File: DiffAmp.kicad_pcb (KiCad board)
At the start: 2 copper layers, 111 parts, among them J1 USB_OTG, J2 Screw_Terminal_1x03, J3 Conn_01x02, J4 Conn_01x02, J5 Conn_01x02, U1 SF_IHXXXXS, U2 TPS7A49, U3 TPS7A30, U4 OPA189, U5 AD8421, U6 OPA189, U7 OPA189

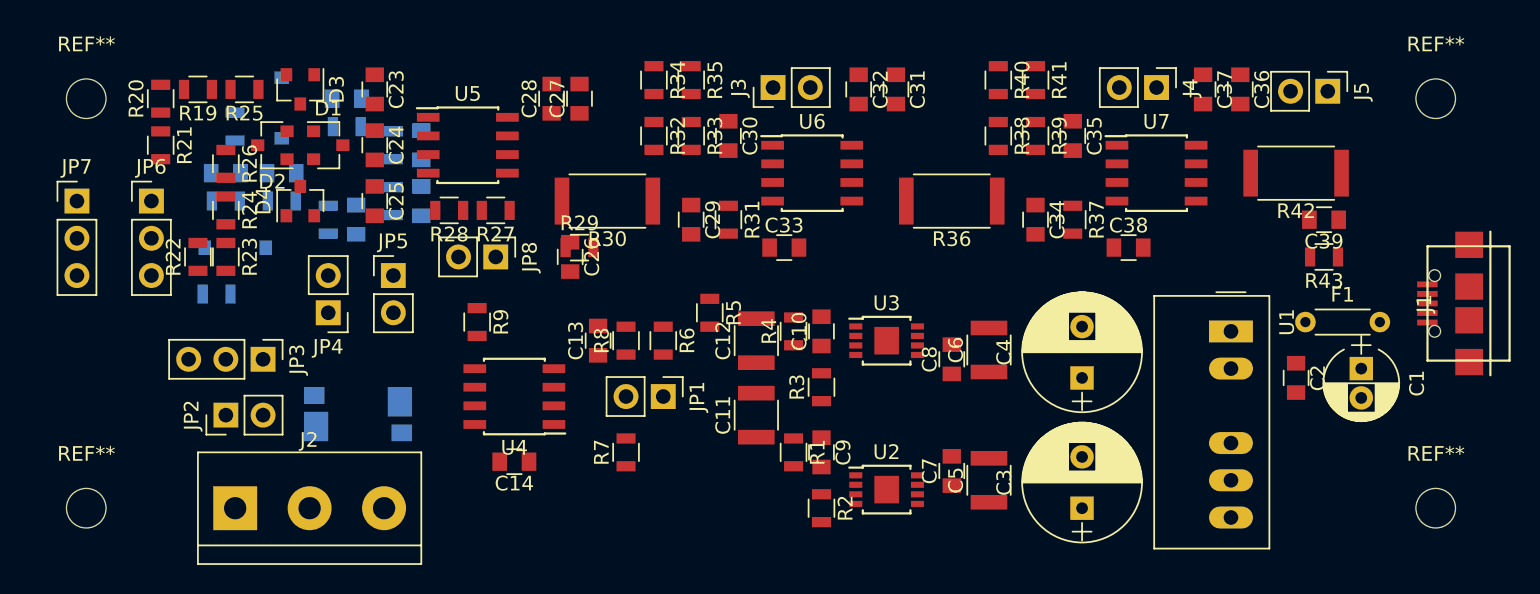
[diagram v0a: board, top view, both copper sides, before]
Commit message: Corrected Board Outline
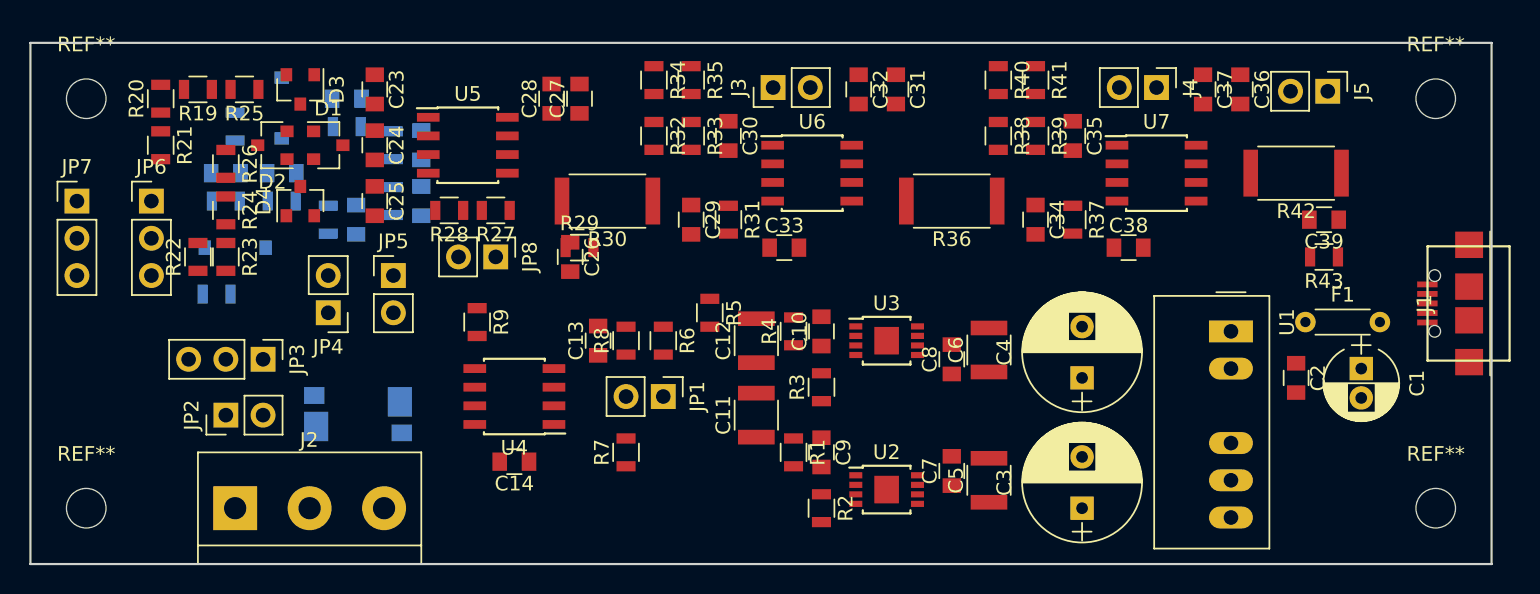
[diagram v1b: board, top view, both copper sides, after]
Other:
- board outline added: 99.7 x 35.6 mm
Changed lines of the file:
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@@
     (pad 1 np_thru_hole circle (at 0 0) (size 2.7 2.7) (drill 2.7) (layers *.Cu *.Mask))
   )
-  (gr_line (start 71.755 59.69) (end 171.45 59.69) (angle 90) (layer Eco2.User) (width 0.2))
-  (gr_line (start 71.755 95.25) (end 71.755 59.69) (angle 90) (layer Eco2.User) (width 0.2))
-  (gr_line (start 171.45 95.25) (end 71.755 95.25) (angle 90) (layer Eco2.User) (width 0.2))
-  (gr_line (start 171.45 95.25) (end 171.45 59.69) (angle 90) (layer Eco2.User) (width 0.2))
+  (gr_line (start 71.755 59.69) (end 71.755 95.25) (angle 90) (layer Edge.Cuts) (width 0.15))
+  (gr_line (start 171.45 59.69) (end 71.755 59.69) (angle 90) (layer Edge.Cuts) (width 0.15))
+  (gr_line (start 171.45 95.25) (end 171.45 59.69) (angle 90) (layer Edge.Cuts) (width 0.15))
+  (gr_line (start 71.755 95.25) (end 171.45 95.25) (angle 90) (layer Edge.Cuts) (width 0.15))
 )

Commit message: Begin Layouting
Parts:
- R10: moved to F.Cu
- moved C26 13.1 mm to (103.5, 62.2), turned to 0 degrees
- moved R10 3.17 mm to (97.8, 86.4)
- moved J3 2.67 mm to (125.1, 62.7), turned to 270 degrees
- moved JP8 2.54 mm to (101.0, 74.3), turned to 90 degrees
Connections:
- J5 pad 2: (no net) -> GNDA
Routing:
- net GNDA: track 0.00 -> 226.5 mm
- net Net-(C11-Pad2): track 0.00 -> 104.0 mm
- net VDDA: track 0.00 -> 62.7 mm
- net VSSA: track 0.00 -> 60.8 mm
- net Net-(C1-Pad2): track 0.00 -> 34.8 mm
- net Net-(JP5-Pad2): track 0.00 -> 31.7 mm, vias 0 -> 1
- net Net-(C4-Pad2): track 0.00 -> 31.6 mm
- net Net-(C3-Pad1): track 0.00 -> 26.7 mm
- net Net-(C20-Pad1): track 0.00 -> 22.2 mm
- net Net-(C35-Pad1): track 0.00 -> 21.6 mm
- net Net-(C30-Pad1): track 0.00 -> 21.4 mm
- net Net-(C24-Pad2): track 0.00 -> 20.1 mm
- net Net-(C1-Pad1): track 0.00 -> 18.6 mm
- net Net-(C23-Pad2): track 0.00 -> 18.3 mm
- net Net-(JP3-Pad2): track 0.00 -> 17.9 mm
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- added copper zone on F.Cu, net Net-(C11-Pad2)

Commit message: Layout Completed
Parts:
- added ?: , DiffAmp:VIA-0.6mm, F.Cu at (119.8, 68.8)
- added ?: , DiffAmp:VIA-0.6mm, F.Cu at (76.8, 74.9)
- added ?: , DiffAmp:VIA-0.6mm, F.Cu at (162.6, 64.8)
- added ?: , DiffAmp:VIA-0.6mm, F.Cu at (162.6, 68.6)
- added ?: , DiffAmp:VIA-0.6mm, F.Cu at (166.4, 68.6)
- added ?: , DiffAmp:VIA-0.6mm, F.Cu at (170.2, 68.6)
- added ?: , DiffAmp:VIA-0.6mm, F.Cu at (170.2, 64.8)
- added ?: , DiffAmp:VIA-0.6mm, F.Cu at (145.4, 61.0)
- added ?: , DiffAmp:VIA-0.6mm, F.Cu at (134.0, 61.0)
- added ?: , DiffAmp:VIA-0.6mm, F.Cu at (126.4, 61.0)
- added ?: , DiffAmp:VIA-0.6mm, F.Cu at (122.6, 61.0)
- added ?: , DiffAmp:VIA-0.6mm, F.Cu at (103.5, 61.0)
- added ?: , DiffAmp:VIA-0.6mm, F.Cu at (79.4, 78.1)
- added ?: , DiffAmp:VIA-0.6mm, F.Cu at (107.3, 61.0)
- added ?: , DiffAmp:VIA-0.6mm, F.Cu at (111.1, 61.0)
- added ?: , DiffAmp:VIA-0.6mm, F.Cu at (97.8, 61.6)
- added ?: , DiffAmp:VIA-0.6mm, F.Cu at (88.3, 61.0)
- added ?: , DiffAmp:VIA-0.6mm, F.Cu at (84.5, 61.0)
- added ?: , DiffAmp:VIA-0.6mm, F.Cu at (80.6, 61.0)
- added ?: , DiffAmp:VIA-0.6mm, F.Cu at (76.8, 61.0)
- added ?: , DiffAmp:VIA-0.6mm, F.Cu at (73.0, 61.0)
- added ?: , DiffAmp:VIA-0.6mm, F.Cu at (150.4, 61.9)
- added ?: , DiffAmp:VIA-0.6mm, F.Cu at (151.8, 61.0)
- added ?: , DiffAmp:VIA-0.6mm, F.Cu at (76.8, 78.1)
- added ?: , DiffAmp:VIA-0.6mm, F.Cu at (158.8, 61.0)
- added ?: , DiffAmp:VIA-0.6mm, F.Cu at (162.6, 61.0)
- added ?: , DiffAmp:VIA-0.6mm, F.Cu at (166.4, 61.0)
- added ?: , DiffAmp:VIA-0.6mm, F.Cu at (118.7, 85.1)
- added ?: , DiffAmp:VIA-0.6mm, F.Cu at (118.7, 82.5)
- added ?: , DiffAmp:VIA-0.6mm, F.Cu at (123.8, 82.5)
- added ?: , DiffAmp:VIA-0.6mm, F.Cu at (134.6, 83.8)
- added ?: , DiffAmp:VIA-0.6mm, F.Cu at (127.6, 82.5)
- added ?: , DiffAmp:VIA-0.6mm, F.Cu at (131.4, 82.5)
- added ?: , DiffAmp:VIA-0.6mm, F.Cu at (137.2, 83.8)
- added ?: , DiffAmp:VIA-0.6mm, F.Cu at (78.1, 74.9)
- added ?: , DiffAmp:VIA-0.6mm, F.Cu at (139.7, 83.8)
- added ?: , DiffAmp:VIA-0.6mm, F.Cu at (139.7, 81.3)
- added ?: , DiffAmp:VIA-0.6mm, F.Cu at (145.4, 81.3)
- added ? (x2): , DiffAmp:VIA-0.6mm, F.Cu at (142.9, 86.4)
- added ?: , DiffAmp:VIA-0.6mm, F.Cu at (139.1, 86.4)
- added ?: , DiffAmp:VIA-0.6mm, F.Cu at (135.3, 86.4)
- added ?: , DiffAmp:VIA-0.6mm, F.Cu at (131.4, 86.4)
- added ?: , DiffAmp:VIA-0.6mm, F.Cu at (120.0, 90.2)
- added ?: , DiffAmp:VIA-0.6mm, F.Cu at (123.8, 90.2)
- added ?: , DiffAmp:VIA-0.6mm, F.Cu at (78.7, 82.5)
- added ?: , DiffAmp:VIA-0.6mm, F.Cu at (123.8, 94.0)
- added ?: , DiffAmp:VIA-0.6mm, F.Cu at (127.6, 94.0)
- added ?: , DiffAmp:VIA-0.6mm, F.Cu at (131.4, 94.0)
- added ?: , DiffAmp:VIA-0.6mm, F.Cu at (135.3, 94.0)
- added ?: , DiffAmp:VIA-0.6mm, F.Cu at (139.1, 94.0)
- added ?: , DiffAmp:VIA-0.6mm, F.Cu at (142.9, 94.0)
- added ?: , DiffAmp:VIA-0.6mm, F.Cu at (150.5, 94.0)
- added ?: , DiffAmp:VIA-0.6mm, F.Cu at (146.7, 94.0)
- added ?: , DiffAmp:VIA-0.6mm, F.Cu at (146.7, 87.6)
- added ?: , DiffAmp:VIA-0.6mm, F.Cu at (146.7, 90.2)
- added ?: , DiffAmp:VIA-0.6mm, F.Cu at (82.5, 90.2)
- added ?: , DiffAmp:VIA-0.6mm, F.Cu at (150.5, 90.2)
- added ?: , DiffAmp:VIA-0.6mm, F.Cu at (150.5, 87.6)
- added ?: , DiffAmp:VIA-0.6mm, F.Cu at (157.5, 88.9)
- added ?: , DiffAmp:VIA-0.6mm, F.Cu at (157.5, 90.8)
- added ?: , DiffAmp:VIA-0.6mm, F.Cu at (157.5, 93.3)
- added ?: , DiffAmp:VIA-0.6mm, F.Cu at (157.5, 86.4)
- added ?: , DiffAmp:VIA-0.6mm, F.Cu at (170.2, 61.0)
- added ?: , DiffAmp:VIA-0.6mm, F.Cu at (82.5, 86.4)
- added ?: , DiffAmp:VIA-0.6mm, F.Cu at (78.7, 86.4)
- added ?: , DiffAmp:VIA-0.6mm, F.Cu at (78.7, 90.2)
- added ?: , DiffAmp:VIA-0.6mm, F.Cu at (73.0, 64.8)
- added ?: , DiffAmp:VIA-0.6mm, F.Cu at (76.2, 66.7)
- added ?: , DiffAmp:VIA-0.6mm, F.Cu at (73.0, 67.3)
- added ?: , DiffAmp:VIA-0.6mm, F.Cu at (73.0, 71.1)
- added ?: , DiffAmp:VIA-0.6mm, F.Cu at (73.0, 74.9)
- added ?: , DiffAmp:VIA-0.6mm, F.Cu at (73.0, 78.7)
- added ?: , DiffAmp:VIA-0.6mm, F.Cu at (73.0, 82.5)
- added ?: , DiffAmp:VIA-0.6mm, F.Cu at (73.0, 86.4)
- added ?: , DiffAmp:VIA-0.6mm, F.Cu at (73.0, 90.2)
- added ?: , DiffAmp:VIA-0.6mm, F.Cu at (88.9, 88.9)
- added ?: , DiffAmp:VIA-0.6mm, F.Cu at (87.0, 88.3)
- added ?: , DiffAmp:VIA-0.6mm, F.Cu at (88.9, 87.0)
- added ?: , DiffAmp:VIA-0.6mm, F.Cu at (78.7, 63.5)
- added ?: , DiffAmp:VIA-0.6mm, F.Cu at (94.6, 86.4)
- added ?: , DiffAmp:VIA-0.6mm, F.Cu at (94.6, 83.8)
- added ?: , DiffAmp:VIA-0.6mm, F.Cu at (101.6, 87.6)
- added ?: , DiffAmp:VIA-0.6mm, F.Cu at (101.6, 91.4)
- added ?: , DiffAmp:VIA-0.6mm, F.Cu at (105.4, 91.4)
- added ?: , DiffAmp:VIA-0.6mm, F.Cu at (73.0, 94.0)
- added ?: , DiffAmp:VIA-0.6mm, F.Cu at (78.7, 94.0)
- added ?: , DiffAmp:VIA-0.6mm, F.Cu at (82.5, 94.0)
- added ?: , DiffAmp:VIA-0.6mm, F.Cu at (86.4, 94.0)
- added ?: , DiffAmp:VIA-0.6mm, F.Cu at (90.2, 94.0)
- added ?: , DiffAmp:VIA-0.6mm, F.Cu at (78.7, 66.0)
- added ?: , DiffAmp:VIA-0.6mm, F.Cu at (94.0, 94.0)
- added ?: , DiffAmp:VIA-0.6mm, F.Cu at (97.8, 94.0)
- added ?: , DiffAmp:VIA-0.6mm, F.Cu at (101.6, 94.0)
- added ?: , DiffAmp:VIA-0.6mm, F.Cu at (99.7, 88.9)
- added ?: , DiffAmp:VIA-0.6mm, F.Cu at (99.7, 85.1)
- added ?: , DiffAmp:VIA-0.6mm, F.Cu at (99.7, 81.3)
- added ?: , DiffAmp:VIA-0.6mm, F.Cu at (96.5, 81.3)
- added ?: , DiffAmp:VIA-0.6mm, F.Cu at (96.5, 80.0)
- added ?: , DiffAmp:VIA-0.6mm, F.Cu at (98.4, 74.9)
- added ?: , DiffAmp:VIA-0.6mm, F.Cu at (100.3, 76.8)
- added ?: , DiffAmp:VIA-0.6mm, F.Cu at (82.5, 70.5)
- added ?: , DiffAmp:VIA-0.6mm, F.Cu at (105.4, 94.0)
- added ?: , DiffAmp:VIA-0.6mm, F.Cu at (113.7, 90.8)
- added ?: , DiffAmp:VIA-0.6mm, F.Cu at (115.6, 90.2)
- added ?: , DiffAmp:VIA-0.6mm, F.Cu at (106.0, 80.6)
- added ?: , DiffAmp:VIA-0.6mm, F.Cu at (105.4, 73.7)
- added ?: , DiffAmp:VIA-0.6mm, F.Cu at (104.1, 76.8)
- added ?: , DiffAmp:VIA-0.6mm, F.Cu at (108.0, 76.8)
- added ?: , DiffAmp:VIA-0.6mm, F.Cu at (109.9, 71.1)
- added ?: , DiffAmp:VIA-0.6mm, F.Cu at (111.8, 69.8)
- added ?: , DiffAmp:VIA-0.6mm, F.Cu at (112.4, 62.2)
- added ?: , DiffAmp:VIA-0.6mm, F.Cu at (78.9, 68.8)
- added ?: , DiffAmp:VIA-0.6mm, F.Cu at (111.8, 64.8)
- added ?: , DiffAmp:VIA-0.6mm, F.Cu at (120.0, 61.0)
- added ?: , DiffAmp:VIA-0.6mm, F.Cu at (120.7, 63.5)
- added ?: , DiffAmp:VIA-0.6mm, F.Cu at (125.7, 69.8)
- added ?: , DiffAmp:VIA-0.6mm, F.Cu at (111.8, 76.8)
- added ?: , DiffAmp:VIA-0.6mm, F.Cu at (115.6, 76.8)
- added ?: , DiffAmp:VIA-0.6mm, F.Cu at (111.8, 73.7)
- added ?: , DiffAmp:VIA-0.6mm, F.Cu at (114.9, 73.7)
- added ?: , DiffAmp:VIA-0.6mm, F.Cu at (118.1, 74.3)
- added ?: , DiffAmp:VIA-0.6mm, F.Cu at (118.1, 75.6)
- added ?: , DiffAmp:VIA-0.6mm, F.Cu at (82.5, 69.2)
- added ?: , DiffAmp:VIA-0.6mm, F.Cu at (123.8, 75.6)
- added ?: , DiffAmp:VIA-0.6mm, F.Cu at (121.3, 75.6)
- added ?: , DiffAmp:VIA-0.6mm, F.Cu at (126.4, 75.6)
- added ?: , DiffAmp:VIA-0.6mm, F.Cu at (130.8, 67.9)
- added ?: , DiffAmp:VIA-0.6mm, F.Cu at (131.4, 65.4)
- added ?: , DiffAmp:VIA-0.6mm, F.Cu at (154.9, 65.4)
- added ?: , DiffAmp:VIA-0.6mm, F.Cu at (130.2, 74.3)
- added ?: , DiffAmp:VIA-0.6mm, F.Cu at (134.0, 74.3)
- added ?: , DiffAmp:VIA-0.6mm, F.Cu at (134.0, 68.6)
- added ?: , DiffAmp:VIA-0.6mm, F.Cu at (134.0, 64.8)
- added ?: , DiffAmp:VIA-0.6mm, F.Cu at (84.5, 65.4)
- added ?: , DiffAmp:VIA-0.6mm, F.Cu at (135.9, 61.0)
- added ?: , DiffAmp:VIA-0.6mm, F.Cu at (135.9, 64.8)
- added ?: , DiffAmp:VIA-0.6mm, F.Cu at (142.9, 69.2)
- added ?: , DiffAmp:VIA-0.6mm, F.Cu at (139.7, 68.6)
- added ?: , DiffAmp:VIA-0.6mm, F.Cu at (135.9, 68.6)
- added ?: , DiffAmp:VIA-0.6mm, F.Cu at (135.9, 76.2)
- added ?: , DiffAmp:VIA-0.6mm, F.Cu at (139.7, 76.2)
- added ?: , DiffAmp:VIA-0.6mm, F.Cu at (143.5, 76.2)
- added ?: , DiffAmp:VIA-0.6mm, F.Cu at (147.3, 76.2)
- added ?: , DiffAmp:VIA-0.6mm, F.Cu at (149.2, 75.6)
- added ?: , DiffAmp:VIA-0.6mm, F.Cu at (82.5, 64.8)
- added ?: , DiffAmp:VIA-0.6mm, F.Cu at (153.7, 71.1)
- added ?: , DiffAmp:VIA-0.6mm, F.Cu at (153.7, 74.3)
- added ?: , DiffAmp:VIA-0.6mm, F.Cu at (157.5, 71.8)
- added ?: , DiffAmp:VIA-0.6mm, F.Cu at (157.5, 74.3)
- added ?: , DiffAmp:VIA-0.6mm, F.Cu at (158.8, 68.6)
- added ?: , DiffAmp:VIA-0.6mm, F.Cu at (158.8, 64.8)
- added ?: , DiffAmp:VIA-0.6mm, F.Cu at (166.4, 70.5)
- added ?: , DiffAmp:VIA-0.6mm, F.Cu at (170.2, 70.5)
- added ?: , DiffAmp:VIA-0.6mm, F.Cu at (163.2, 70.5)
- added ?: , DiffAmp:VIA-0.6mm, F.Cu at (163.2, 74.3)
- moved J4 0.13 mm to (148.6, 62.9)
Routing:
- net VSSA: track 60.8 -> 199.4 mm, vias 0 -> 7
- net VDDA: track 62.7 -> 191.3 mm, vias 0 -> 8
- net GNDA: track 226.5 -> 278.7 mm, vias 0 -> 2
- net Net-(C11-Pad2): track 104.0 -> 125.2 mm
- net Net-(J1-Pad6): track 0.00 -> 8.00 mm
- added copper zone on B.Cu, net GNDA
- added copper zone on F.Cu, net GNDA
- added copper zone on B.Cu, net Net-(C11-Pad2)
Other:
- board text added: "Differential Amplifier V0.1 David Krebs 03/2018"
- board text added: "Dir|Div"
- board text added: "EXT R|INT R"
- board text added: "GND"
- board text added: "IN+|IN-"
- board text added: "Inp.Div"
- board text added: "Out1|GND"
- board text added: "Out2|GND"
- board text added: "Out3|GND"
- board text added: "o: x10 c: x100"

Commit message: Silkscreen corrected
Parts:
- removed the ? at (145.4, 61.0)
- removed the ? at (122.6, 61.0)
- moved ? 2.25 mm to (164.1, 62.6)
- moved ? 2.07 mm to (128.4, 60.6)
- moved ? 1.08 mm to (78.6, 77.3)
- moved ? 1.05 mm to (106.9, 76.6)
- moved ? 0.25 mm to (119.8, 61.0)

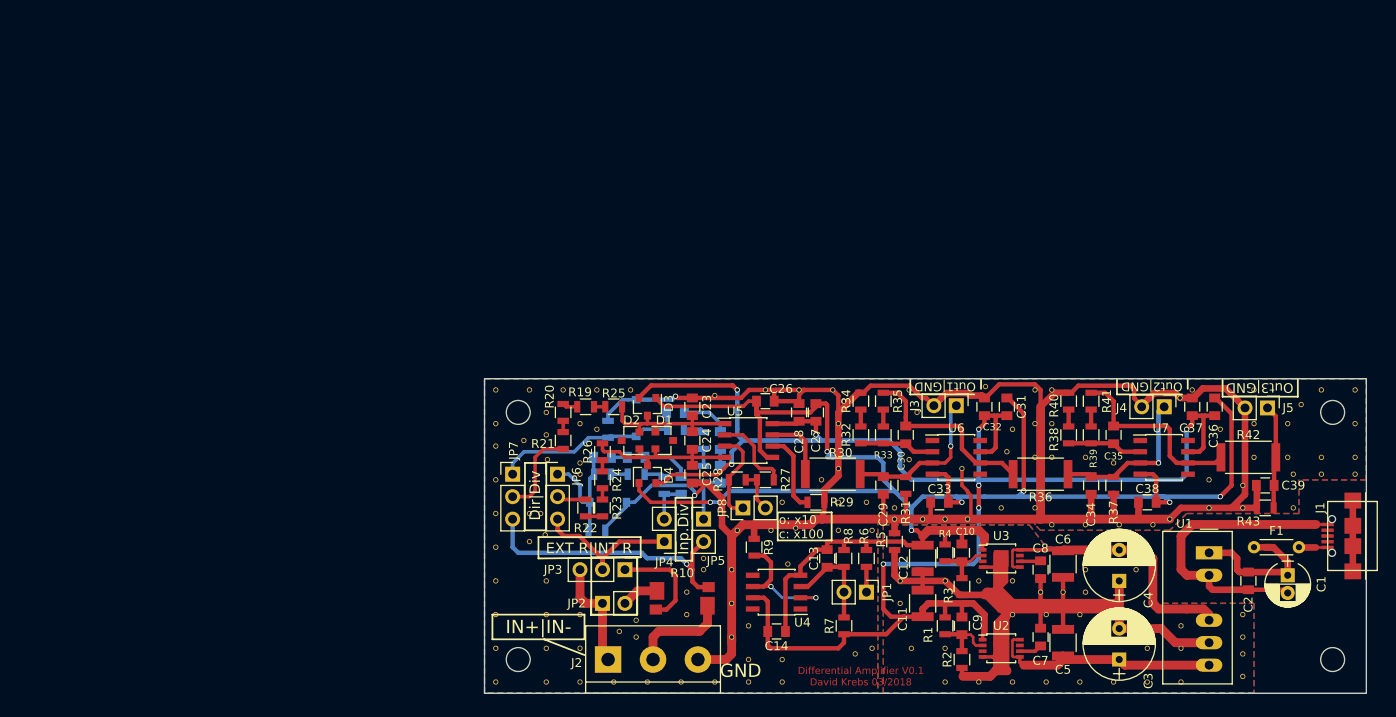
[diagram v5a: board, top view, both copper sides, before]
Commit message: Added PCB Assembly Drawing
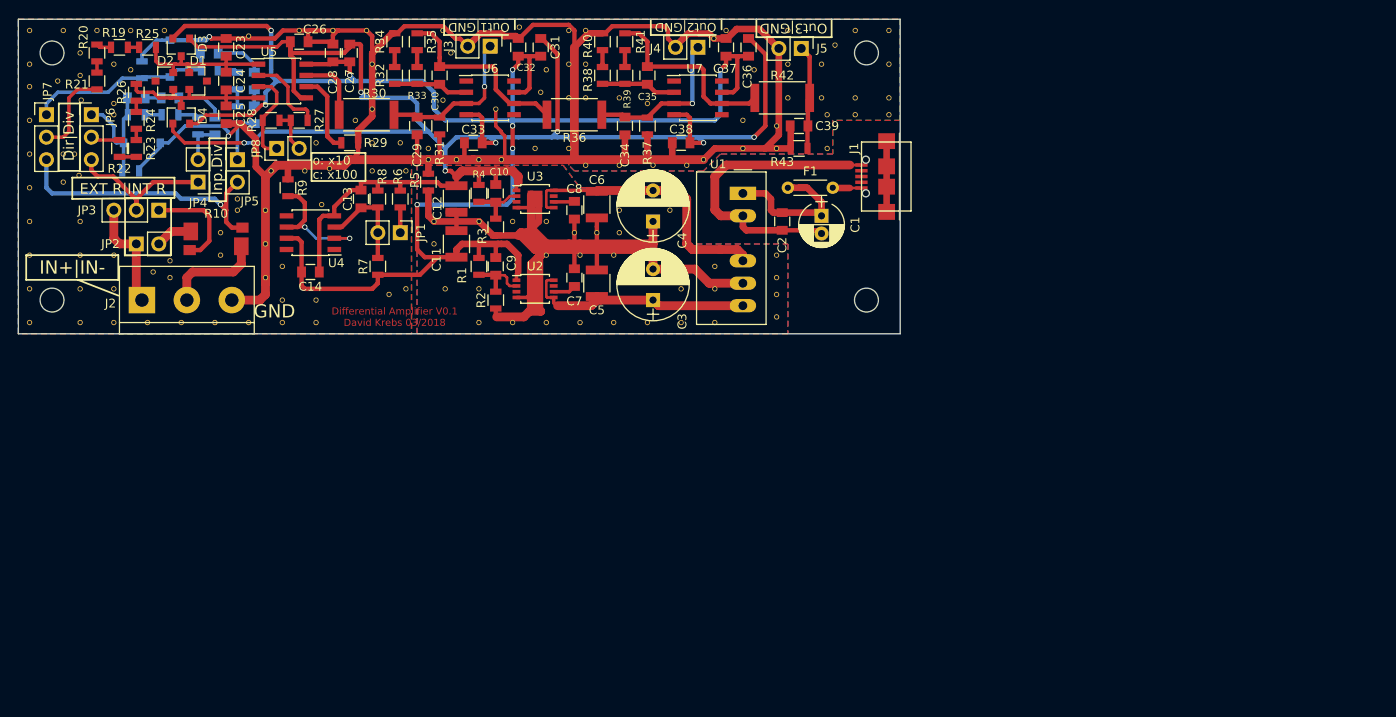
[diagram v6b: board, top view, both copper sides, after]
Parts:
- F1: footprint Resistors_THT:R_Axial_DIN0204_L3.6mm_D1.6mm_P5.08mm_Horizontal -> DiffAmp:R_Axial_DIN0204_L3.6mm_D1.6mm_P5.08mm_Horizontal
- moved ? 66.6 mm to (25.4, 34.3)
- moved ? 66.6 mm to (20.3, 34.3)
- moved ? 66.6 mm to (36.2, 48.3)
- moved ? 66.6 mm to (36.2, 46.4)
- moved ? 66.6 mm to (61.0, 50.2)
- moved R6 66.6 mm to (62.2, 39.4)
- moved ? 66.6 mm to (67.1, 28.2)
- moved ? 66.6 mm to (24.1, 34.3)
- moved ? 66.6 mm to (109.9, 24.1)
- moved ? 66.6 mm to (109.9, 27.9)
- moved ? 66.6 mm to (113.7, 27.9)
- moved ? 66.6 mm to (117.5, 27.9)
- moved ? 66.6 mm to (117.5, 24.1)
- moved ? 66.6 mm to (81.3, 20.3)
- moved ? 66.6 mm to (75.7, 19.9)
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
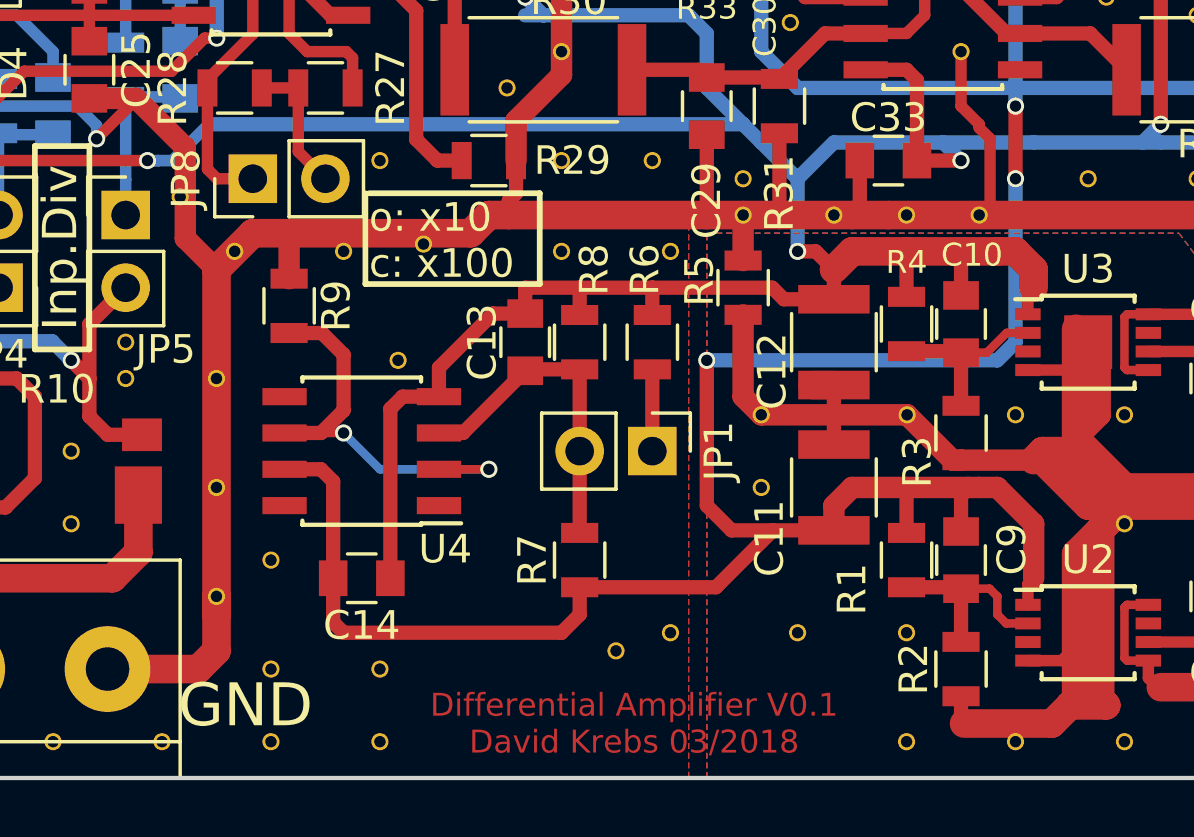
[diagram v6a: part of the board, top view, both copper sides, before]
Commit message: Changed GNDA-"Generation" on Schematic and Board
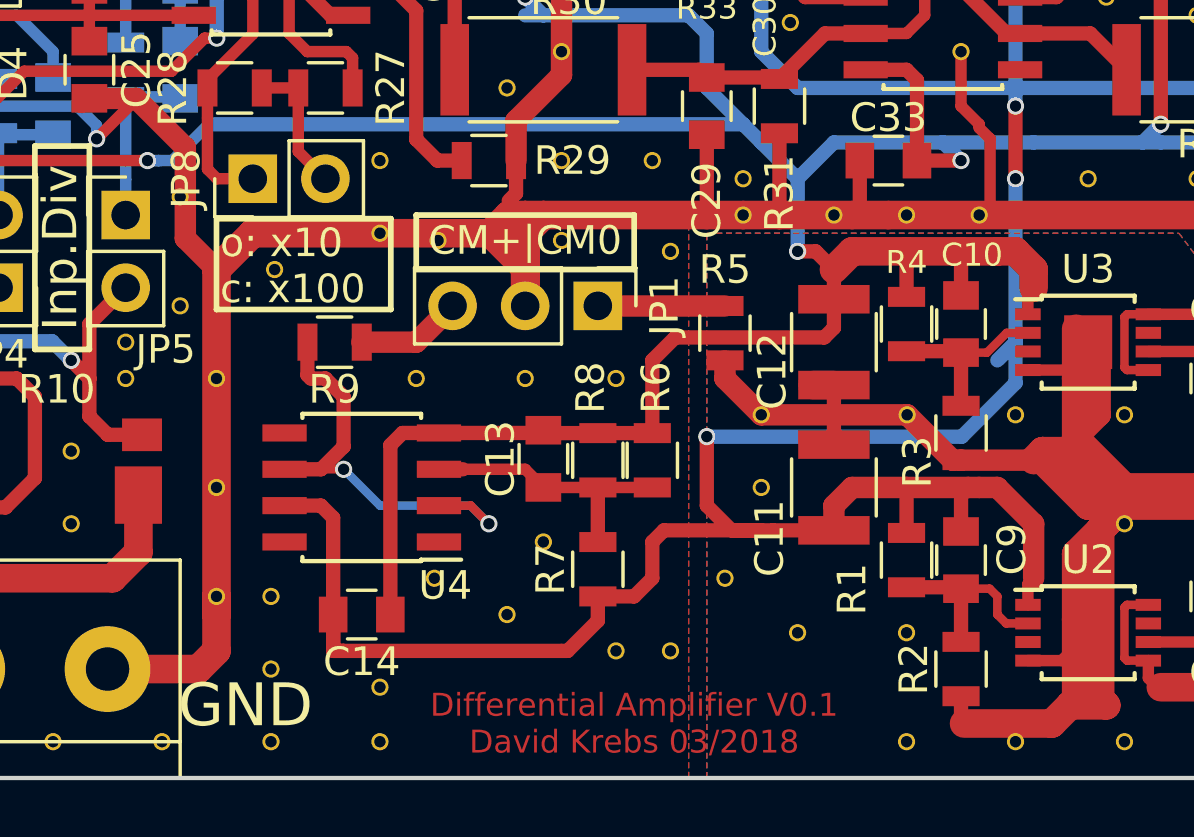
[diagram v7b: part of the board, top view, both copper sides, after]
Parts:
- added ?: , DiffAmp:VIA-0.6mm, F.Cu at (64.8, 47.6)
- added ?: , DiffAmp:VIA-0.6mm, F.Cu at (61.0, 50.2)
- added ?: , DiffAmp:VIA-0.6mm, F.Cu at (54.7, 35.8)
- added ?: , DiffAmp:VIA-0.6mm, F.Cu at (57.8, 40.6)
- added ?: , DiffAmp:VIA-0.6mm, F.Cu at (61.0, 40.6)
- added ?: , DiffAmp:VIA-0.6mm, F.Cu at (58.4, 46.4)
- added ?: , DiffAmp:VIA-0.6mm, F.Cu at (54.6, 47.6)
- JP1: value Jumper_NO_Small -> Jumper_NC_Dual; footprint Pin_Headers:Pin_Header_Straight_1x02_Pitch2.54mm -> Pin_Headers:Pin_Header_Straight_1x03_Pitch2.54mm
- moved JP1 5.43 mm to (60.3, 38.1)
- moved ? 5.28 mm to (49.0, 36.8)
- moved R8 4.18 mm to (60.3, 43.5)
- moved R6 4.13 mm to (62.2, 43.5)
- moved C13 4.13 mm to (58.4, 43.5)
- moved ? 4.02 mm to (57.1, 48.9)
- moved ? 2.69 mm to (45.7, 38.1)
- moved R9 2.03 mm to (51.1, 39.4), turned to 180 degrees
- moved R5 1.71 mm to (64.8, 39.1)
- moved ? 1.42 mm to (52.7, 35.6)
- moved C14 1.27 mm to (52.1, 48.9)
- moved U4 1.27 mm to (52.1, 44.5)
- moved ? 1.27 mm to (48.9, 48.3)
- moved ? 0.90 mm to (54.0, 40.6)
- moved R7 0.71 mm to (60.3, 47.3)
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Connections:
- JP1 pad 2: Net-(C13-Pad1) -> GNDA
- R5 pad 1: GNDA -> Net-(JP1-Pad1)
- R6 pad 2: Net-(JP1-Pad1) -> Net-(C13-Pad1)
- R9 pad 1: GNDA -> Net-(JP1-Pad3)
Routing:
- net GNDA: track 278.7 -> 283.4 mm
- net Net-(JP1-Pad3): track 0.00 -> 3.70 mm
- net VDDA: track 191.3 -> 193.5 mm
- net Net-(JP1-Pad1): track 2.86 -> 4.45 mm
- net Net-(C11-Pad2): track 125.2 -> 123.8 mm
- net Net-(C13-Pad1): track 11.6 -> 10.5 mm
- net Net-(R9-Pad2): track 16.0 -> 16.8 mm
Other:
- board text added: "CM+|CM0"
